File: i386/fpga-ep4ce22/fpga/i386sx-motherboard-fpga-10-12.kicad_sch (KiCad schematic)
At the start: 49 parts, among them U3 (4/6) EP4CE22F17C8N, Y1 25MHz XO

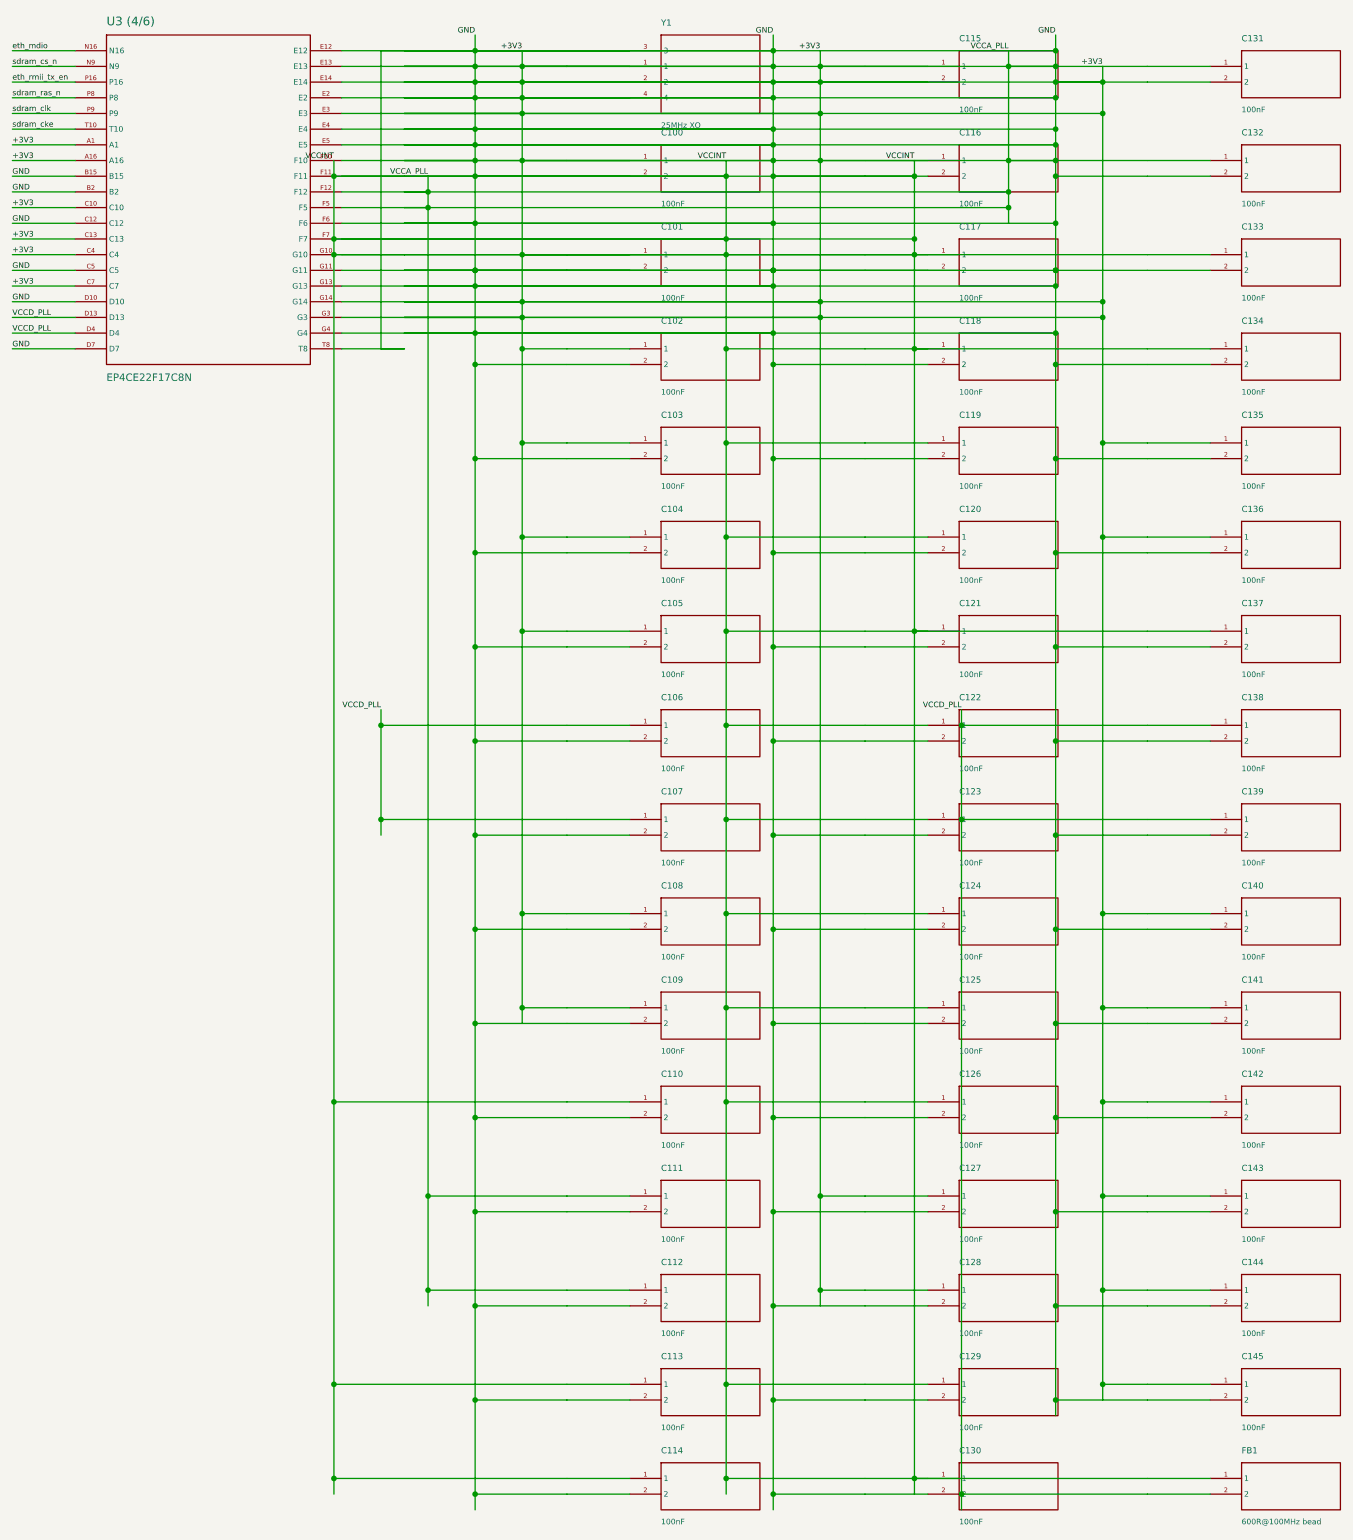
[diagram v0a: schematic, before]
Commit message: Publish the motherboards' KiCad files
From socket3@c0f6464 socket7@9205469 socket370@524f5b1 i386@bea926c
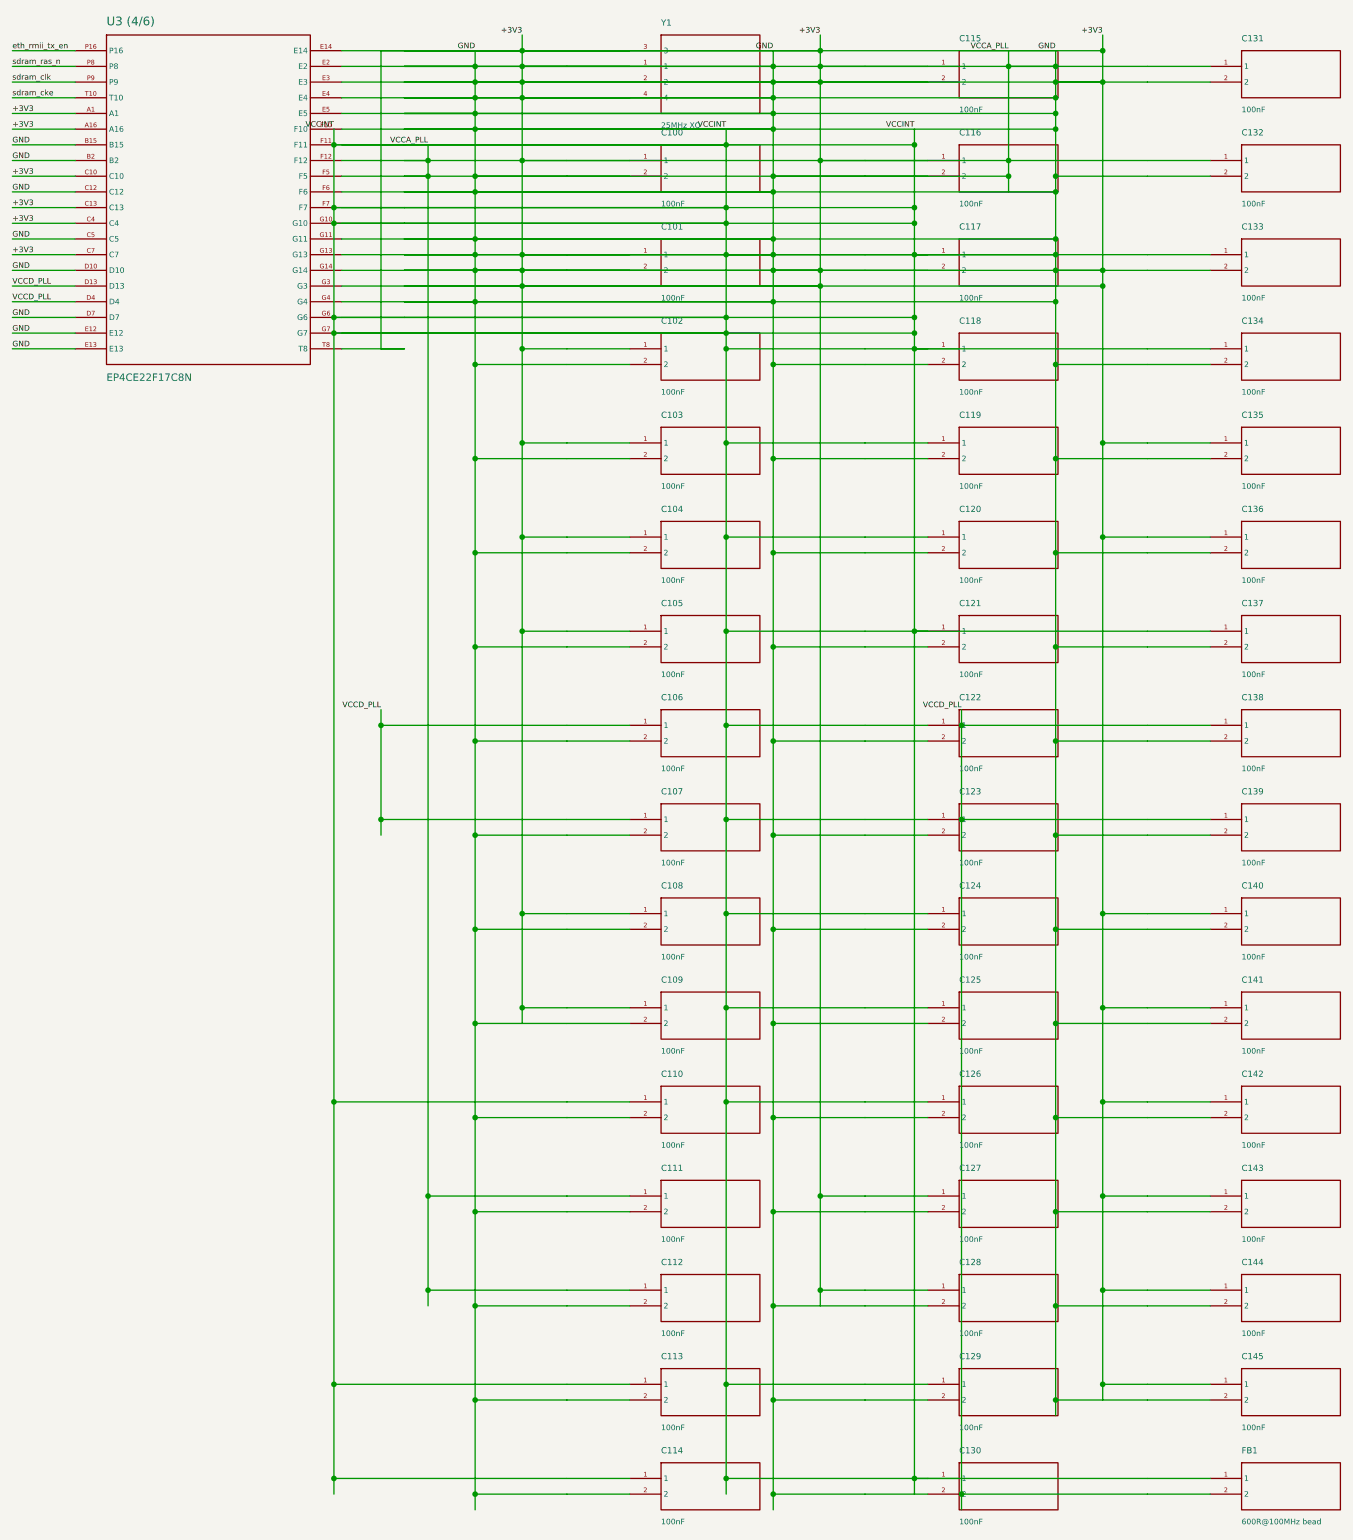
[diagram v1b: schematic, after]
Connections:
- net +3V3: now also U3 (4/6).G6, U3 (4/6).G7
- removed net eth_mdio: U3 (4/6).N16
- removed net sdram_cs_n: U3 (4/6).N9
